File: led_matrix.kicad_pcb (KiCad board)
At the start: 2 copper layers, 85.1 x 109.2 mm, 116 parts, among them J1 I2C, J2 Extra, J3 Address, J4 +5V, J5 GND, J6 Power Input, J7 Columns, J8 Row Addr., Q1 2N3904, Q2 2N3904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

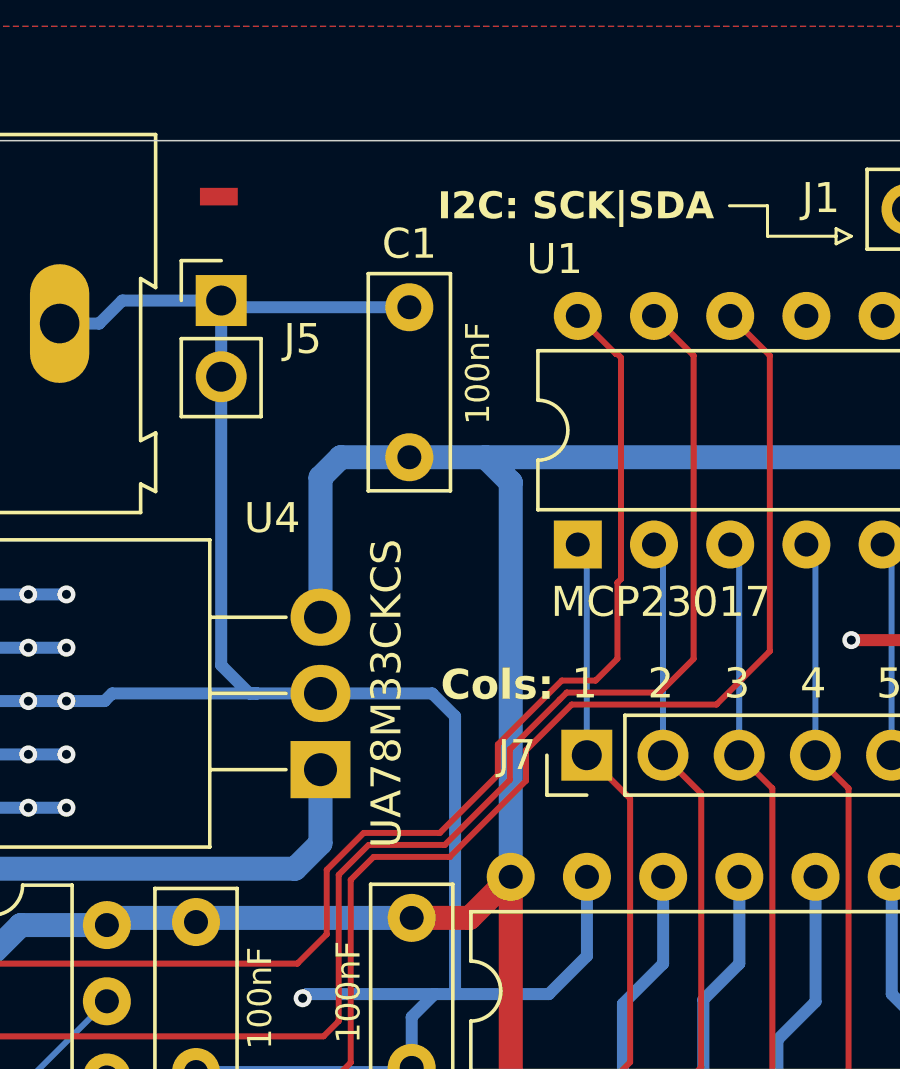
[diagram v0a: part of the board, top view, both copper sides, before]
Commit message: Added an header to pick VCC after the regulator
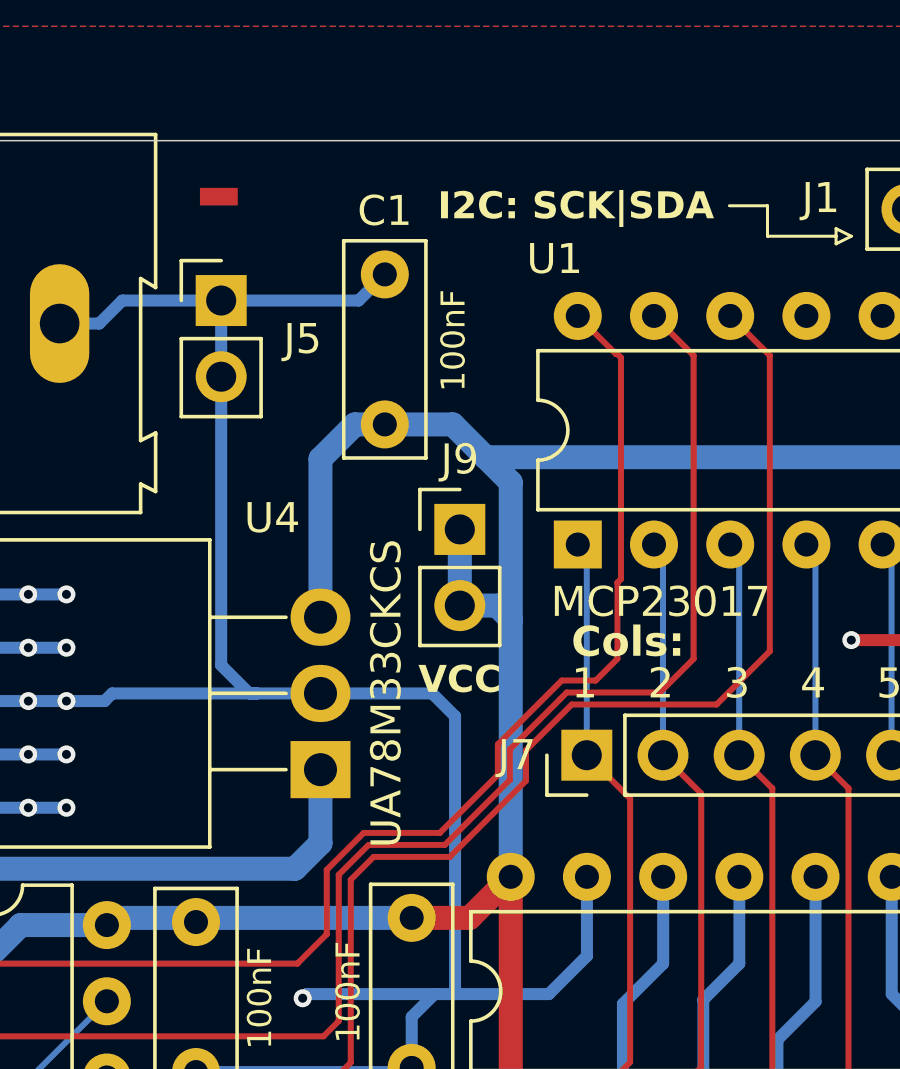
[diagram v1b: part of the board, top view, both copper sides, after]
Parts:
- added J9: VCC, Connector_PinHeader_2.54mm:PinHeader_1x02_P2.54mm_Vertical, F.Cu at (133.0, 56.0)
- moved C1 1.37 mm to (130.5, 52.5)
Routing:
- net VCC: track 149.7 -> 155.4 mm

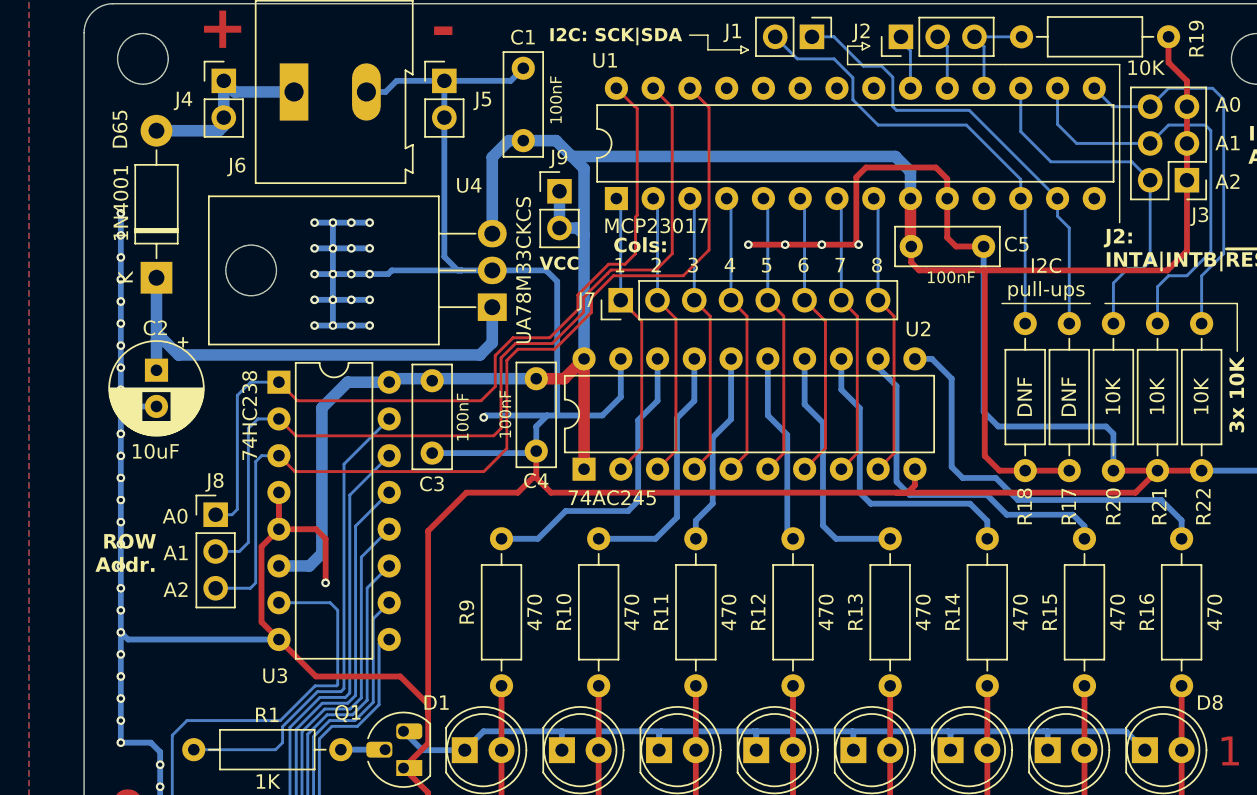
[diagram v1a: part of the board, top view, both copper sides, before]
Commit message: Added resistor networks on PCB
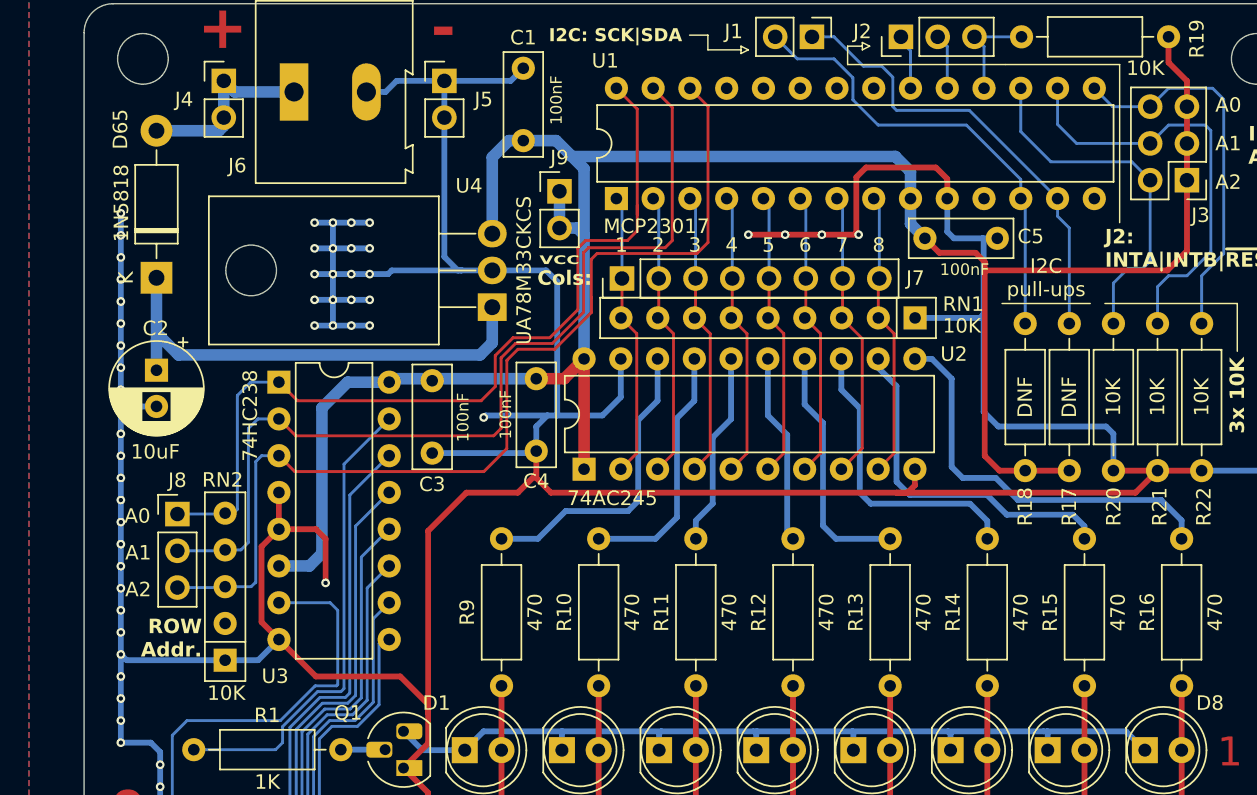
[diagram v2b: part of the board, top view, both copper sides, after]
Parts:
- added RN1: 10K, Resistor_THT:R_Array_SIP9, F.Cu at (157.6, 64.8)
- added RN2: 10K, Resistor_THT:R_Array_SIP5, F.Cu at (109.9, 88.4)
- D65: value 1N4001 -> 1N5818
- moved J8 2.64 mm to (106.6, 78.3)
- moved J7 1.50 mm to (137.3, 62.0)
- moved C5 1.10 mm to (158.2, 59.2)
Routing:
- net GND: track 551.1 -> 556.9 mm
- net /R_ADDR_0: track 56.1 -> 60.4 mm
- net /R_ADDR_1: track 61.1 -> 65.0 mm
- net /R_ADDR_2: track 65.5 -> 69.3 mm
- net VCC: track 155.4 -> 154.2 mm

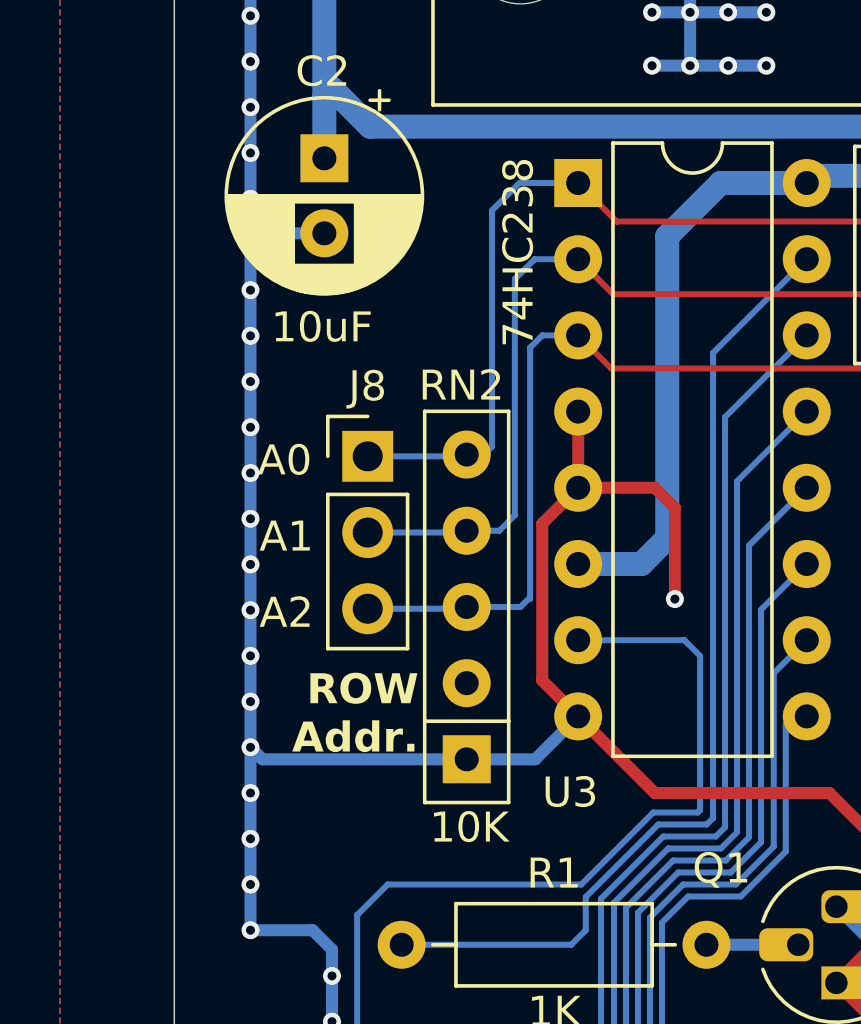
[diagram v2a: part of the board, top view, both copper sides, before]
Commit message: Moved around some components
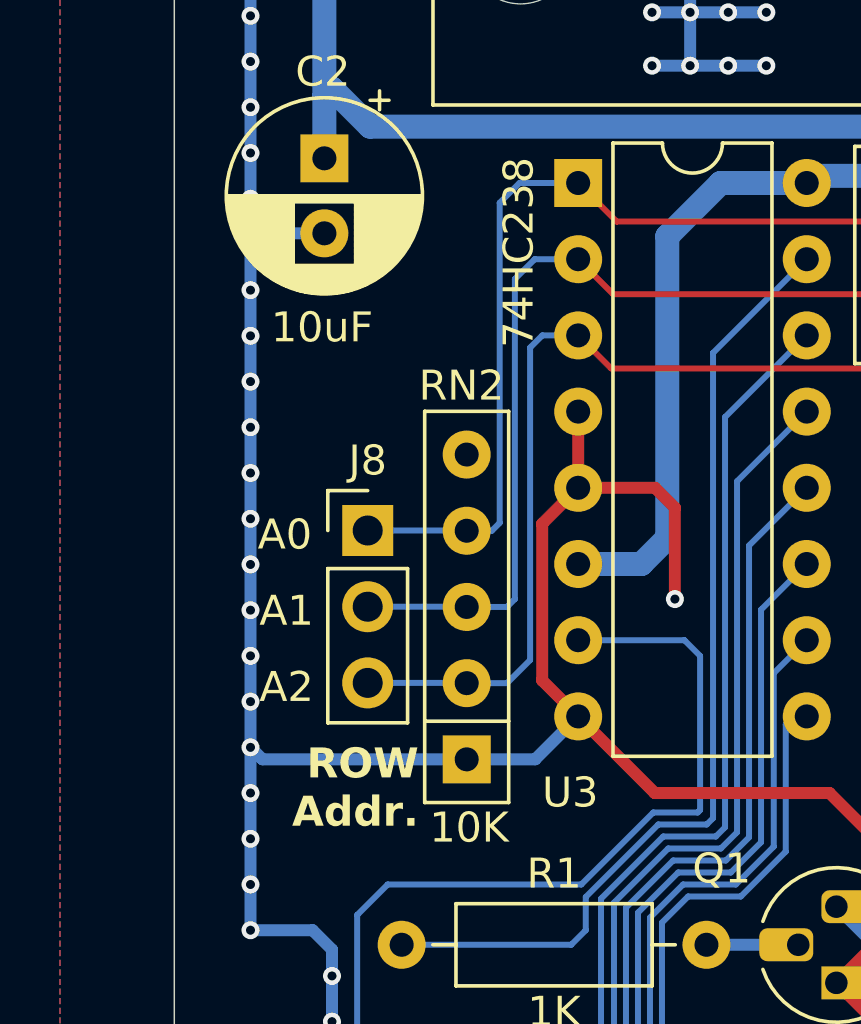
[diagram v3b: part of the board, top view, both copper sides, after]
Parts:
- moved J8 2.47 mm to (106.6, 80.8)
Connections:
- RN2 pad 2: unconnected-(RN2-R1-Pad2) -> /R_ADDR_2
- RN2 pad 3: /R_ADDR_2 -> /R_ADDR_1
- RN2 pad 4: /R_ADDR_1 -> /R_ADDR_0
- RN2 pad 5: /R_ADDR_0 -> unconnected-(RN2-R4-Pad5)
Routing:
- net /R_ADDR_0: track 60.4 -> 63.2 mm
- net /R_ADDR_1: track 65.0 -> 67.8 mm
- net /R_ADDR_2: track 69.3 -> 71.5 mm
- net unconnected-(RN2-R4-Pad5): track 0.00 -> 0.67 mm
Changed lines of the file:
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@@
 	(net 69 "/B_COL_7")
 	(net 70 "/RECT_5V")
-	(net 71 "unconnected-(RN2-R1-Pad2)")
+	(net 71 "unconnected-(RN2-R4-Pad5)")
 	(footprint "LED_THT:LED_D5.0mm"
 		(layer "F.Cu")
@@
 	(footprint "Connector_PinHeader_2.54mm:PinHeader_1x03_P2.54mm_Vertical"
 		(layer "F.Cu")
-		(at 106.6 78.3)
+		(at 106.6 80.772)
 		(descr "Through hole straight pin header, 1x03, 2.54mm pitch, single row")
 		(tags "Through hole pin header THT 1x03 2.54mm single row")
@@
 		(tags "R")
 		(property "Reference" "RN1"
-			(at -3.33 0.95 360)
+			(at -3.33 0.95 0)
 			(layer "F.SilkS")
 			(effects
@@
 		)
 		(fp_text user "${REFERENCE}"
-			(at 10.16 0 360)
+			(at 10.16 0 0)
 			(layer "F.Fab")
 			(effects
@@
 			(layers "*.Cu" "*.Mask")
 			(remove_unused_layers no)
-			(net 71 "unconnected-(RN2-R1-Pad2)")
+			(net 53 "/R_ADDR_2")
 			(pinfunction "R1")
-			(pintype "passive+no_connect")
+			(pintype "passive")
 		)
 		(pad "3" thru_hole oval
@@
 			(layers "*.Cu" "*.Mask")
 			(remove_unused_layers no)
-			(net 53 "/R_ADDR_2")
+			(net 54 "/R_ADDR_1")
 			(pinfunction "R2")
 			(pintype "passive")
@@
 			(layers "*.Cu" "*.Mask")
 			(remove_unused_layers no)
-			(net 54 "/R_ADDR_1")
+			(net 52 "/R_ADDR_0")
 			(pinfunction "R3")
 			(pintype "passive")
@@
 			(layers "*.Cu" "*.Mask")
 			(remove_unused_layers no)
-			(net 52 "/R_ADDR_0")
+			(net 71 "unconnected-(RN2-R4-Pad5)")
 			(pinfunction "R4")
-			(pintype "passive")
+			(pintype "passive+no_connect")
 		)
 		(model "${KICAD8_3DMODEL_DIR}/Resistor_THT.3dshapes/R_Array_SIP5.wrl"
@@
 	)
 	(gr_text "A2"
-		(at 104.8 83.518286 0)
+		(at 104.8 85.990286 0)
 		(layer "F.SilkS")
 		(effects
@@
 	)
 	(gr_text "A1"
-		(at 104.8 80.978286 0)
+		(at 104.8 83.450286 0)
 		(layer "F.SilkS")
 		(effects
@@
 	)
 	(gr_text "A0"
-		(at 104.744428 78.438286 0)
+		(at 104.744428 80.910286 0)
 		(layer "F.SilkS")
 		(effects
@@
 	)
 	(gr_text "ROW\nAddr."
-		(at 108.3 86.872286 0)
+		(at 108.3 89.344286 0)
 		(layer "F.SilkS")
 		(effects
@@
 	)
 	(segment
-		(start 111.659286 69.188714)
-		(end 113.615572 69.188714)
+		(start 110.738 80.78)
+		(end 111 80.518)
 		(width 0.2)
 		(layer "B.Cu")
@@
 	)
 	(segment
-		(start 110.744 70.104)
+		(start 111 69.848)
 		(end 111.659286 69.188714)
 		(width 0.2)
@@
 	)
 	(segment
-		(start 109.9 78.24)
-		(end 110.482 78.24)
+		(start 111.659286 69.188714)
+		(end 113.615572 69.188714)
 		(width 0.2)
 		(layer "B.Cu")
@@
 	)
 	(segment
-		(start 110.744 77.978)
-		(end 110.744 70.104)
+		(start 106.6 80.772)
+		(end 109.892 80.772)
 		(width 0.2)
 		(layer "B.Cu")
@@
 	)
 	(segment
-		(start 106.6 78.3)
-		(end 109.84 78.3)
+		(start 109.892 80.772)
+		(end 109.9 80.78)
 		(width 0.2)
 		(layer "B.Cu")
@@
 	)
 	(segment
-		(start 110.482 78.24)
-		(end 110.744 77.978)
+		(start 109.84 80.84)
+		(end 109.9 80.78)
 		(width 0.2)
 		(layer "B.Cu")
@@
 	)
 	(segment
-		(start 109.84 78.3)
-		(end 109.9 78.24)
+		(start 109.9 80.78)
+		(end 110.738 80.78)
+		(width 0.2)
+		(layer "B.Cu")
+		(net 52)
+	)
+	(segment
+		(start 111 80.518)
+		(end 111 69.848)
 		(width 0.2)
 		(layer "B.Cu")
@@
 	)
 	(segment
-		(start 112.014 83.058)
-		(end 112.014 83)
-		(width 0.2)
-		(layer "B.Cu")
-		(net 53)
-	)
-	(segment
-		(start 106.6 83.38)
-		(end 109.84 83.38)
+		(start 112.014 74.676)
+		(end 112.014 85.09)
 		(width 0.2)
 		(layer "B.Cu")
@@
 	)
 	(segment
-		(start 109.9 83.32)
-		(end 111.694 83.32)
+		(start 112.014 85.09)
+		(end 111.244 85.86)
 		(width 0.2)
 		(layer "B.Cu")
@@
 	)
 	(segment
-		(start 112.421286 74.268714)
-		(end 113.615572 74.268714)
+		(start 109.892 85.852)
+		(end 109.9 85.86)
 		(width 0.2)
 		(layer "B.Cu")
@@
 	)
 	(segment
-		(start 112.014 83)
-		(end 112.014 74.676)
+		(start 111.244 85.86)
+		(end 109.9 85.86)
 		(width 0.2)
 		(layer "B.Cu")
@@
 	)
 	(segment
-		(start 111.694 83.32)
-		(end 112.014 83)
+		(start 106.6 85.852)
+		(end 109.892 85.852)
 		(width 0.2)
 		(layer "B.Cu")
@@
 	)
 	(segment
-		(start 109.84 83.38)
-		(end 109.9 83.32)
+		(start 112.421286 74.268714)
+		(end 112.014 74.676)
 		(width 0.2)
 		(layer "B.Cu")
@@
 	)
 	(segment
-		(start 112.014 74.676)
+		(start 113.615572 74.268714)
 		(end 112.421286 74.268714)
 		(width 0.2)
@@
 	)
 	(segment
-		(start 110.99 80.78)
-		(end 111.506 80.264)
+		(start 113.600572 71.743714)
+		(end 113.615572 71.728714)
 		(width 0.2)
 		(layer "B.Cu")
@@
 	)
 	(segment
-		(start 113.600572 71.743714)
-		(end 113.615572 71.728714)
+		(start 111.506 83.058)
+		(end 111.244 83.32)
 		(width 0.2)
 		(layer "B.Cu")
@@
 	)
 	(segment
-		(start 106.6 80.84)
-		(end 109.84 80.84)
+		(start 106.6 83.312)
+		(end 109.892 83.312)
 		(width 0.2)
 		(layer "B.Cu")
@@
 	)
 	(segment
-		(start 111.506 72.39)
-		(end 112.167286 71.728714)
+		(start 112.167286 71.728714)
+		(end 111.506 72.39)
 		(width 0.2)
 		(layer "B.Cu")
@@
 	)
 	(segment
-		(start 112.167286 71.728714)
-		(end 113.615572 71.728714)
+		(start 109.84 83.38)
+		(end 109.9 83.32)
 		(width 0.2)
 		(layer "B.Cu")
@@
 	)
 	(segment
-		(start 109.84 80.84)
-		(end 109.9 80.78)
+		(start 111.506 72.39)
+		(end 111.506 83.058)
 		(width 0.2)
 		(layer "B.Cu")
@@
 	)
 	(segment
-		(start 111.506 80.264)
-		(end 111.506 72.39)
+		(start 109.892 83.312)
+		(end 109.9 83.32)
 		(width 0.2)
 		(layer "B.Cu")
@@
 	)
 	(segment
-		(start 109.9 80.78)
-		(end 110.99 80.78)
+		(start 113.615572 71.728714)
+		(end 112.167286 71.728714)
+		(width 0.2)
+		(layer "B.Cu")
+		(net 54)
+	)
+	(segment
+		(start 111.244 83.32)
+		(end 109.9 83.32)
 		(width 0.2)
 		(layer "B.Cu")
@@
 		(net 70)
 	)
+	(segment
+		(start 109.9 78.24)
+		(end 110.482 78.24)
+		(width 0.2)
+		(layer "B.Cu")
+		(net 71)
+	)
+	(segment
+		(start 109.84 78.3)
+		(end 109.9 78.24)
+		(width 0.2)
+		(layer "B.Cu")
+		(net 71)
+	)
 	(zone
